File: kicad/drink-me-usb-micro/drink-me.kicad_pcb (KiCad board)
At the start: 2 copper layers, 94 x 29 mm, 20 parts, among them J0 AVR-ISP-6, J1 USB_mini_micro_B, K0 KEYSW, K1 KEYSW, K2 KEYSW, K3 KEYSW, SW1 RESET, U1 32U2-AU, Y1 16Mhz

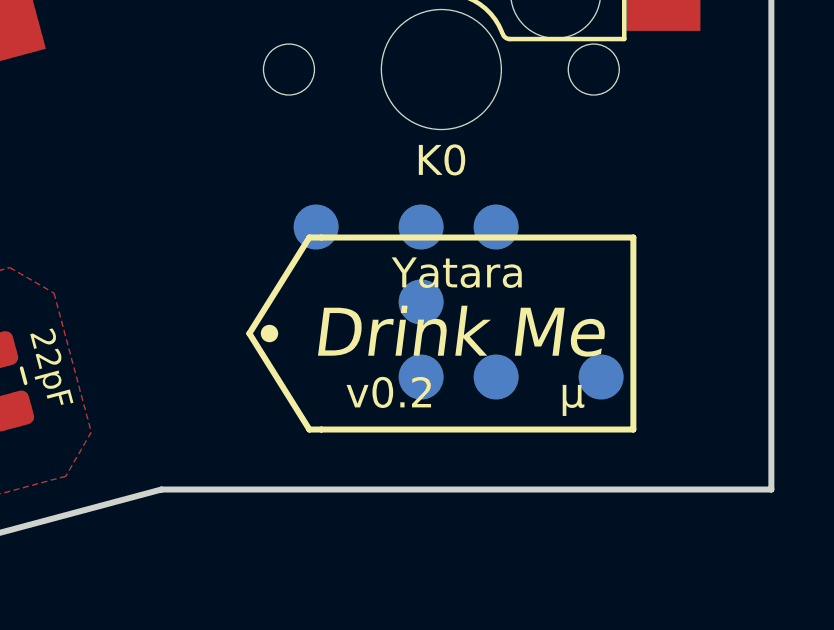
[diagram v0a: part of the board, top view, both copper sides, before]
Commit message: Use HRO TYPE-C-31-M-12 USB-C connector. Add bill of materials. Add printed back part without rest, including tolerance adjustments.
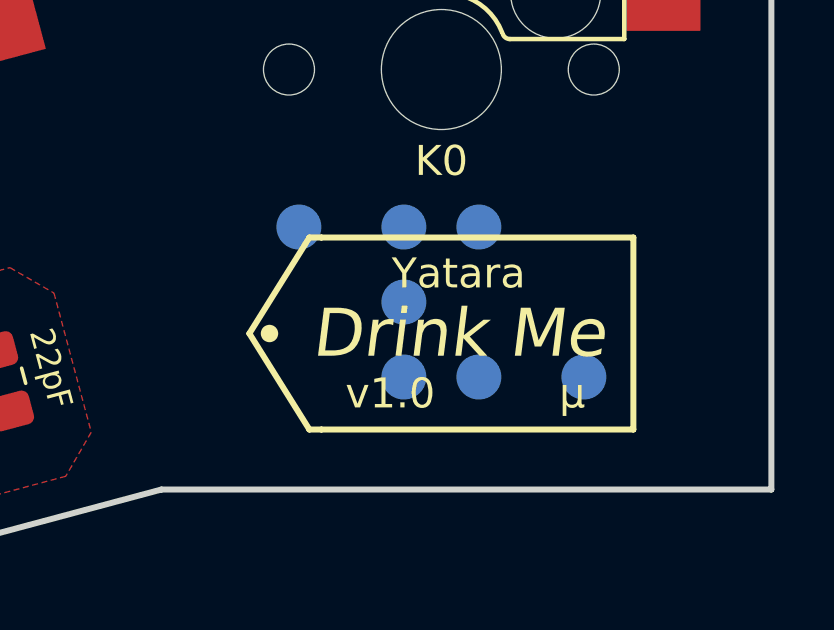
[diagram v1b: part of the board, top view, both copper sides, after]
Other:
- board text added: "JLCJLCJLCJLC"
- board text added: "v1.0"
- board text removed: "v0.2"
